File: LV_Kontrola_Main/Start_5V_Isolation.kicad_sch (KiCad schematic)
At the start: 56 parts, among them IC1 UCC12040DVE, IC11 UCC12040DVE, IC13 UCC12040DVE, IC15 UCC12040DVE, IC3 UCC12040DVE, IC5 UCC12040DVE, IC7 UCC12040DVE, IC9 UCC12040DVE

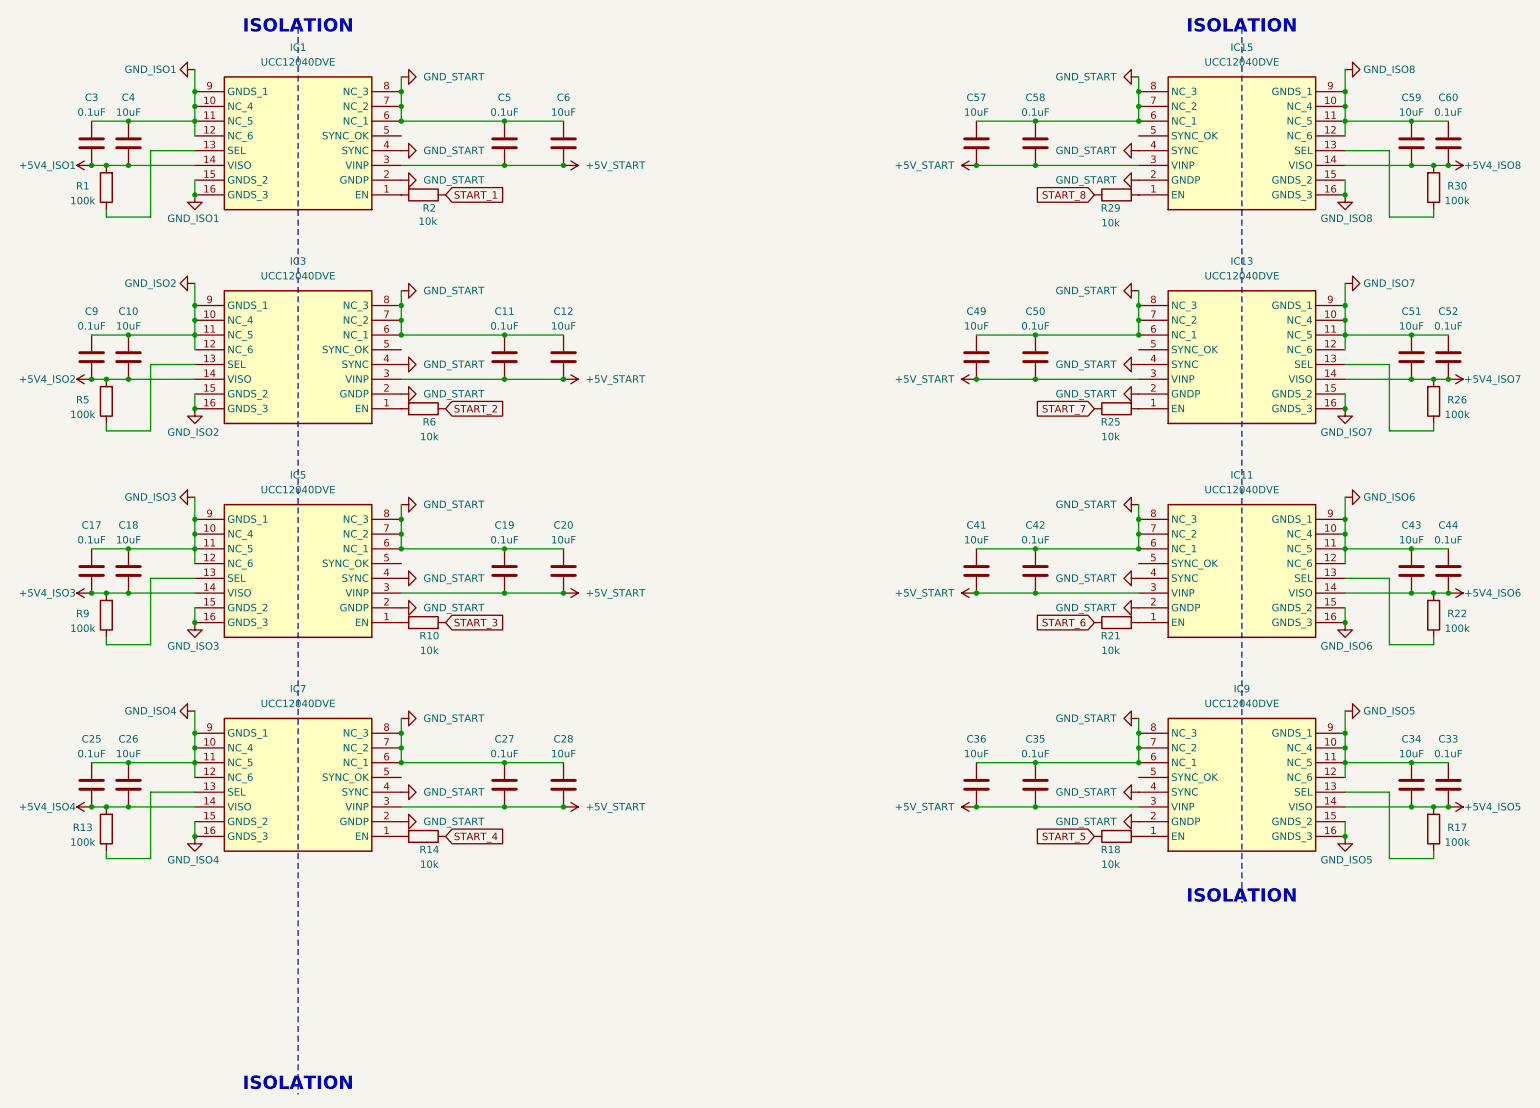
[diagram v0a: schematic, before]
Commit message: Changes to LV_Kontrola_Main
Added a lot to the schematic, fixed component libs, mics...
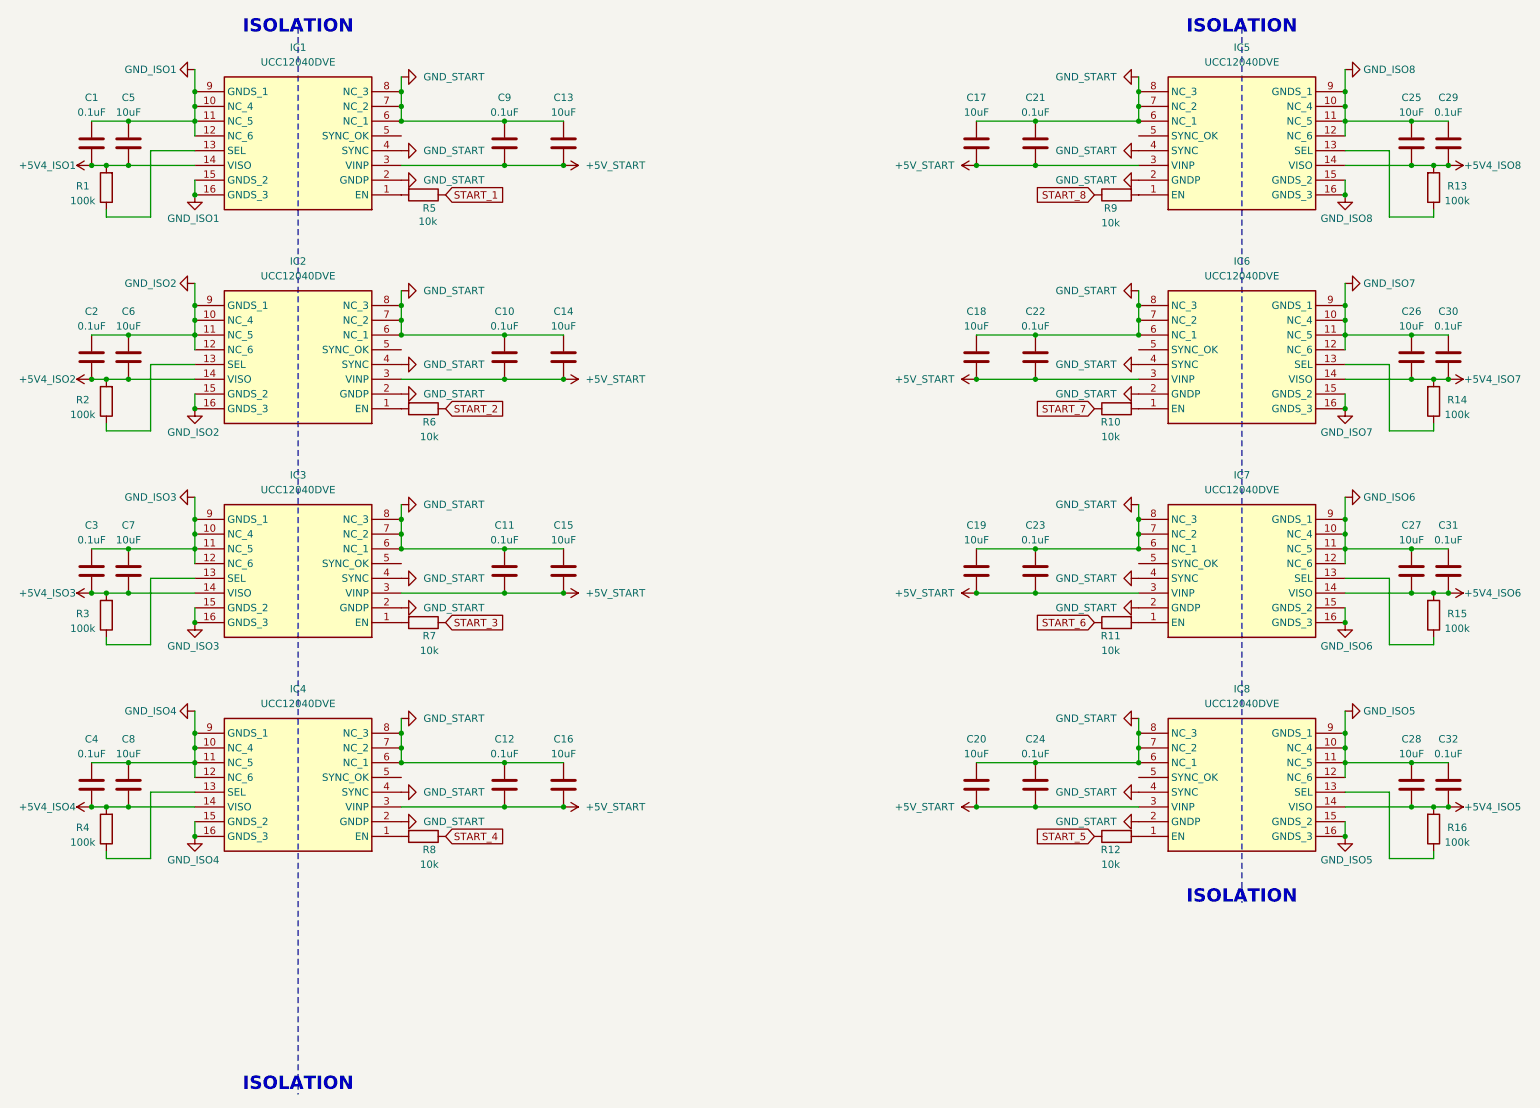
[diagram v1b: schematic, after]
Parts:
- removed C3: 0.1uF, symbol Device:C
- removed C4, C6: 10uF, symbol Device:C
- removed R2: 10k, symbol Device:R
- added C1, C9: 0.1uF, symbol Device:C
- added C13: 10uF, symbol Device:C
- added R5: 10k, symbol Device:R
- C5: value 0.1uF -> 10uF
- renumbered C11 to C10, C19 to C11, C27 to C12, C12 to C14, C20 to C15, C28 to C16, C57 to C17, C49 to C18, C41 to C19, C9 to C2, C36 to C20, C58 to C21, C50 to C22, C42 to C23, C35 to C24, C59 to C25, C51 to C26, C43 to C27, C34 to C28, C60 to C29, C17 to C3, C52 to C30, C44 to C31, C33 to C32, C25 to C4, C10 to C6, C18 to C7, C26 to C8, IC3 to IC2, IC5 to IC3, IC7 to IC4, IC15 to IC5, IC13 to IC6, IC11 to IC7, IC9 to IC8, R25 to R10, R21 to R11, R18 to R12, R30 to R13, R26 to R14, R22 to R15, R17 to R16, R5 to R2, R9 to R3, R13 to R4, R10 to R7, R14 to R8, R29 to R9
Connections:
- net +5V4_ISO1: now also C5.1, C1.1
- net +5V_START: now also C13.1, C9.1; no longer C5.1
- net GND_ISO1: now also C5.2, C1.2
- net GND_START: now also C13.2, C9.2; no longer C5.2
- net START_1: now also R5.1
- net at IC1.1 (EN): now also R5.2
